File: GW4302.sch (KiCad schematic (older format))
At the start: 37 parts, among them J1 C64, J2 JTAG, U1 M5LV-PQFP100, U2 DRAM_2Mx8, U3 LD1117S33

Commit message: As submitted to JLC
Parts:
- removed JP1: Mode, Connector_PinHeader_2.54mm:PinHeader_1x02_P2.54mm_Vertical_SMD_Pin1Left, symbol Device:Jumper_NO_Small
- removed JP2: Size, Connector_PinHeader_2.54mm:PinHeader_2x02_P2.54mm_Vertical_SMD, symbol Connector_Generic:Conn_02x02_Odd_Even
- removed U1: M5LV-PQFP100, stdpads:PQFP-100_14x20mm_P0.65mm, symbol GW_PLD:M5LV-PQFP-100
- removed U2: DRAM_2Mx8, stdpads:SOJ-28-300mil, symbol GW_RAM:DRAM-2Mx8-SOP-28
- added C15, C16, C17, C18, C19, C20, C21, C22, C23, C24, C25, C26, C27, C28, C29, C30, C31, C35, C36, C37: 2u2, stdpads:C_0603, symbol Device:C_Small
- added C3: 10u, stdpads:C_0805, symbol Device:C_Small
- added C32, C33, C34, C38, C39: 22p, stdpads:C_0603, symbol Device:C_Small
- added H5: (no value), stdpads:PasteHole_1.152mm_NPTH, symbol Mechanical:MountingHole_Pad
- added J2: microUSB, stdpads:USB_Micro-B_ShouHan_MicroXNJ, symbol Connector:USB_B_Micro
- added R10: 47, stdpads:R_0603, symbol Device:R_Small
- added R11, R12, R13, R14, R15: 10k, stdpads:R_0603, symbol Device:R_Small
- added R16: 1k, stdpads:R_0603, symbol Device:R_Small
- added U1, U2, U4, U5: 74AHC245PW, stdpads:TSSOP-20_4.4x6.5mm_P0.65mm, symbol GW_Logic:74245
- added U10, U6: 74AHC125PW, stdpads:TSSOP-14_4.4x5mm_P0.65mm, symbol GW_Logic:74125
- added U11, U12, U7: 74LVC1G04GW, stdpads:SOT-353, symbol GW_Logic:741G04GW
- added U13: CH340G, stdpads:SOIC-16_3.9mm, symbol Interface_USB:CH340G
- added U8: LCMXO2-640-TG100, stdpads:TQFP-100_14x14mm_P0.5mm, symbol GW_PLD:LCMXO2-640-TG100
- added U9: W9825G6KH-6, stdpads:TSOP-II-54_22.2x10.16mm_P0.8mm, symbol GW_RAM:SDRAM-16Mx16-TSOP2-54
- added Y1: 12M, stdpads:Crystal_HC49-SMD, symbol Device:Crystal_Small
- C1, C2, C4, C5, C6: value 2u2 -> 10u; LCSC Part (none) -> C15850
- C10, C11, C12, C13, C8, C9: footprint stdpads:C_0805 -> stdpads:C_0603; LCSC Part (none) -> C23630
- C14: value 10p -> 2u2; footprint stdpads:C_0805 -> stdpads:C_0603; LCSC Part (none) -> C23630
- C7: value 2u2 -> 22p; footprint stdpads:C_0805 -> stdpads:C_0603; LCSC Part (none) -> C1653
- H3, H4: footprint stdpads:PasteHole_1.1mm_PTH -> stdpads:PasteHole_1.152mm_NPTH
- J2: footprint Connector:Tag-Connect_TC2050-IDC-NL_2x05_P1.27mm_Vertical -> Connector:Tag-Connect_TC2050-IDC-FP_2x05_P1.27mm_Vertical
- R1, R2: value 0 -> 1k; footprint stdpads:R_0805 -> stdpads:R_0603; LCSC Part (none) -> C21190
- R3: value 1k -> 47; footprint stdpads:R_0805 -> stdpads:R_0603; LCSC Part (none) -> C23182
- R4: value 470 -> 10k; footprint stdpads:R_0805 -> stdpads:R_0603; LCSC Part (none) -> C25804
- R5: value 22k -> 1k; footprint stdpads:R_0805 -> stdpads:R_0603; LCSC Part (none) -> C21190
- R6, R7: value 22k -> 47; footprint stdpads:R_0805 -> stdpads:R_0603; LCSC Part (none) -> C23182
- R8, R9: value 22k -> 10k; footprint stdpads:R_0805 -> stdpads:R_0603; LCSC Part (none) -> C25804
- U3: LCSC Part (none) -> C108494
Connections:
- net labels added: ACLK, ADIR, A~OE~, BA0, BA1, BA10, BA11, BA12, BA13, BA14, BA15, BA2, BA3, BA4, BA5, BA6, BA7, BA8, BA9, BBA, BD0, BD1, BD2, BD3, BD4, BD5, BD6, BD7, BPHI2, BR~W~, B~IO1~, B~IO2~, B~RESET~, DDIR, DMAR~W~, DMA~OE~, DONE, D~OE~, IRQ~OE~, JTAG~OE~, RA12, RBA0, RBA1, RCKE, RCLK, RDQMH, RDQML, RESET~OE~, RW~OE~, R~CS~, TCKr, USB5V, UTCK, UTCKb, UTDI, UTMS, U~TCK~, ~INIT~, ~JTAGEN~, ~PROG~
- net labels removed: R~OE~, Size0, Size1, VMEM, ~Mode~
- wire segments 93 -> 138
- no-connect marks 23 -> 14
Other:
- moved on the sheet: C1, C2, C4, C5, FID1, FID2, FID3, FID4, H1, H2, H3, H4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

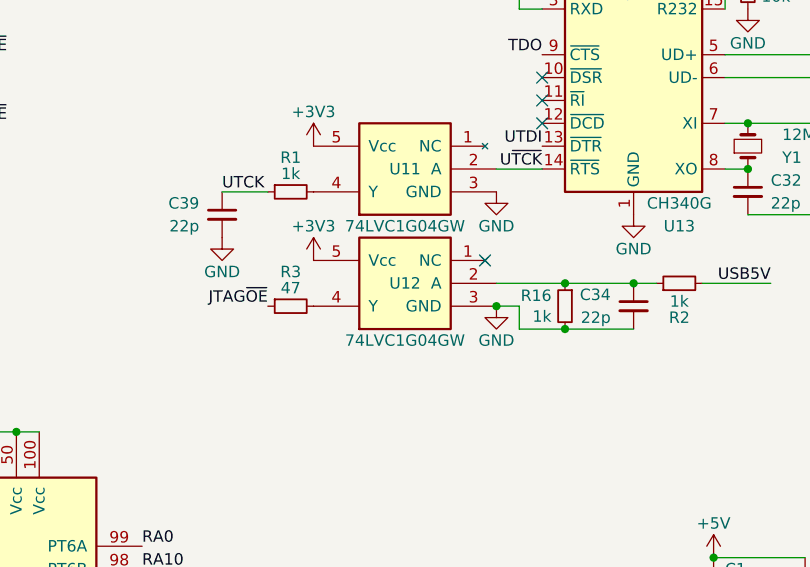
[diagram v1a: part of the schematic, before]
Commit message: Update GW4302.sch
Change from 'LVC to 'AHC for non-edge triggered signal buffering
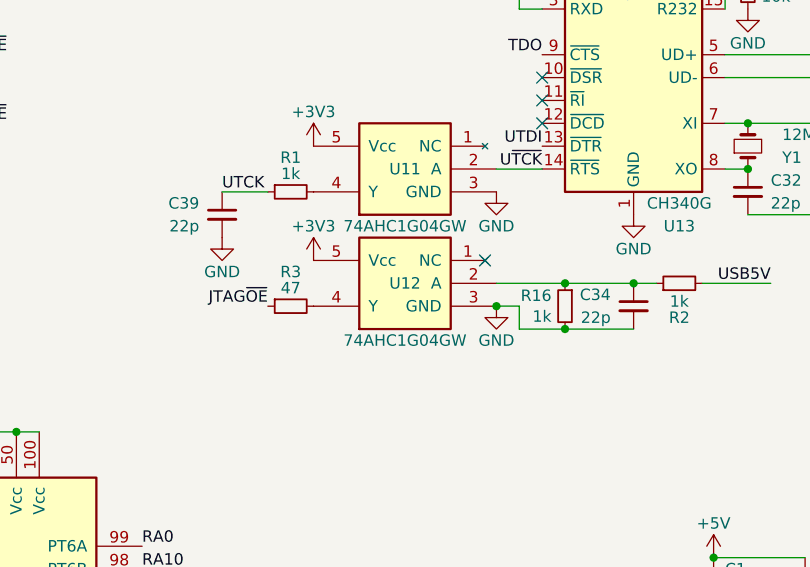
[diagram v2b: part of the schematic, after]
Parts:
- U11, U12: value 74LVC1G04GW -> 74AHC1G04GW; LCSC Part C10237 -> C148197
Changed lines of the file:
@@
 P 6850 1850
 F 0 "U11" H 6850 1850 50  0000 C CNN
-F 1 "74LVC1G04GW" H 6850 1600 50  0000 C CNN
+F 1 "74AHC1G04GW" H 6850 1600 50  0000 C CNN
 F 2 "stdpads:SOT-353" H 6850 1550 50  0001 C TNN
 F 3 "" H 6850 1650 60  0001 C CNN
-F 4 "C10237" H 6850 1850 50  0001 C CNN "LCSC Part"
+F 4 "C148197" H 6850 1850 50  0001 C CNN "LCSC Part"
 	1    6850 1850
 	-1   0    0    -1
@@
 P 6850 2350
 F 0 "U12" H 6850 2350 50  0000 C CNN
-F 1 "74LVC1G04GW" H 6850 2100 50  0000 C CNN
+F 1 "74AHC1G04GW" H 6850 2100 50  0000 C CNN
 F 2 "stdpads:SOT-353" H 6850 2050 50  0001 C TNN
 F 3 "" H 6850 2150 60  0001 C CNN
-F 4 "C10237" H 6850 2350 50  0001 C CNN "LCSC Part"
+F 4 "C148197" H 6850 2350 50  0001 C CNN "LCSC Part"
 	1    6850 2350
 	-1   0    0    -1

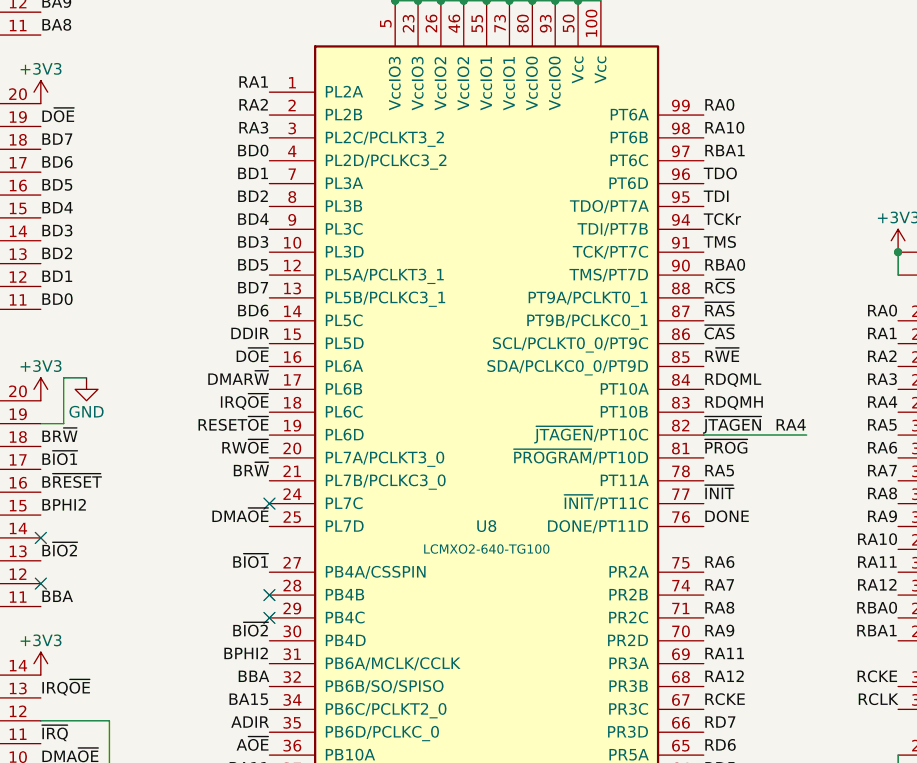
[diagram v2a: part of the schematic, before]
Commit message: Fix JTAG connections on board
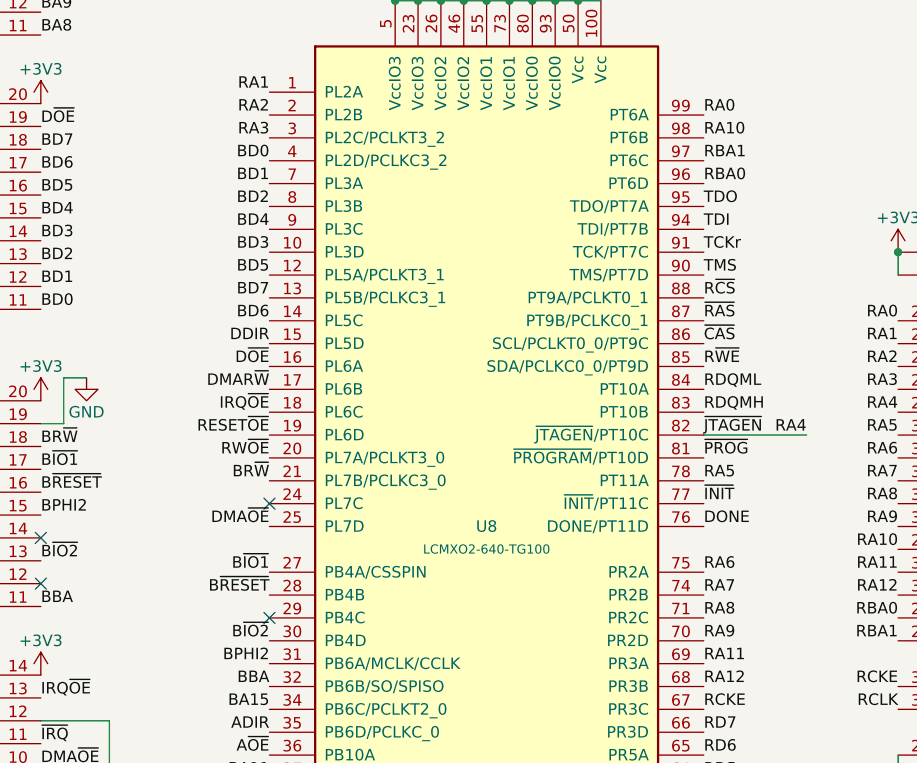
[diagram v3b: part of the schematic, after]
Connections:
- net B~RESET~: now also U8.28 (PB4B)
- net RBA0: now also U8.96 (PT6D); no longer U8.90 (TMS/PT7D)
- net TCKr: now also U8.91 (TCK/PT7C); no longer U8.94 (TDI/PT7B)
- net TDI: now also U8.94 (TDI/PT7B); no longer U8.95 (TDO/PT7A)
- net TDO: now also U8.95 (TDO/PT7A); no longer U8.96 (PT6D)
- net TMS: now also U8.90 (TMS/PT7D); no longer U8.91 (TCK/PT7C)
- no-connect marks 14 -> 13
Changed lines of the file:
@@
 Text Label 7550 5700 0    50   ~ 0
 RDQML
-Text Label 5700 4200 0    50   ~ 0
+Text Label 5700 3800 0    50   ~ 0
 RBA0
 Text Label 5700 3700 0    50   ~ 0
@@
 Wire Wire Line
 	1450 4850 1050 4850
+Text Label 5700 4100 0    50   ~ 0
+TCKr
+Text Label 5700 4200 0    50   ~ 0
+TMS
 Text Label 5700 4000 0    50   ~ 0
-TCKr
-Text Label 5700 4100 0    50   ~ 0
-TMS
+TDI
 Text Label 5700 3900 0    50   ~ 0
-TDI
-Text Label 5700 3800 0    50   ~ 0
 TDO
 Text Label 5700 4900 0    50   ~ 0
@@
 NoConn ~ 3800 5200
 NoConn ~ 3800 5700
-NoConn ~ 3800 5600
 Text Label 2800 6550 0    50   ~ 0
 ~DMA~
 NoConn ~ 8950 1550
+Text Label 3800 5600 2    50   ~ 0
+B~RESET~
 $EndSCHEMATC
